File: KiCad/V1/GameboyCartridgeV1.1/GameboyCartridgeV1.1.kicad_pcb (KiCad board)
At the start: 2 copper layers, 52.8 x 61.2 mm, 58 parts, among them J1 USB_C_Receptacle_USB2.0, J2 DBG_UART, J3 Conn_01x06, Q1 CJ2302, SW1 SW_Push, U1 W25Q128JVS, U2 RP2040, U3 CartBus, U5 TXB0102DCU, U6 TXB0108PW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

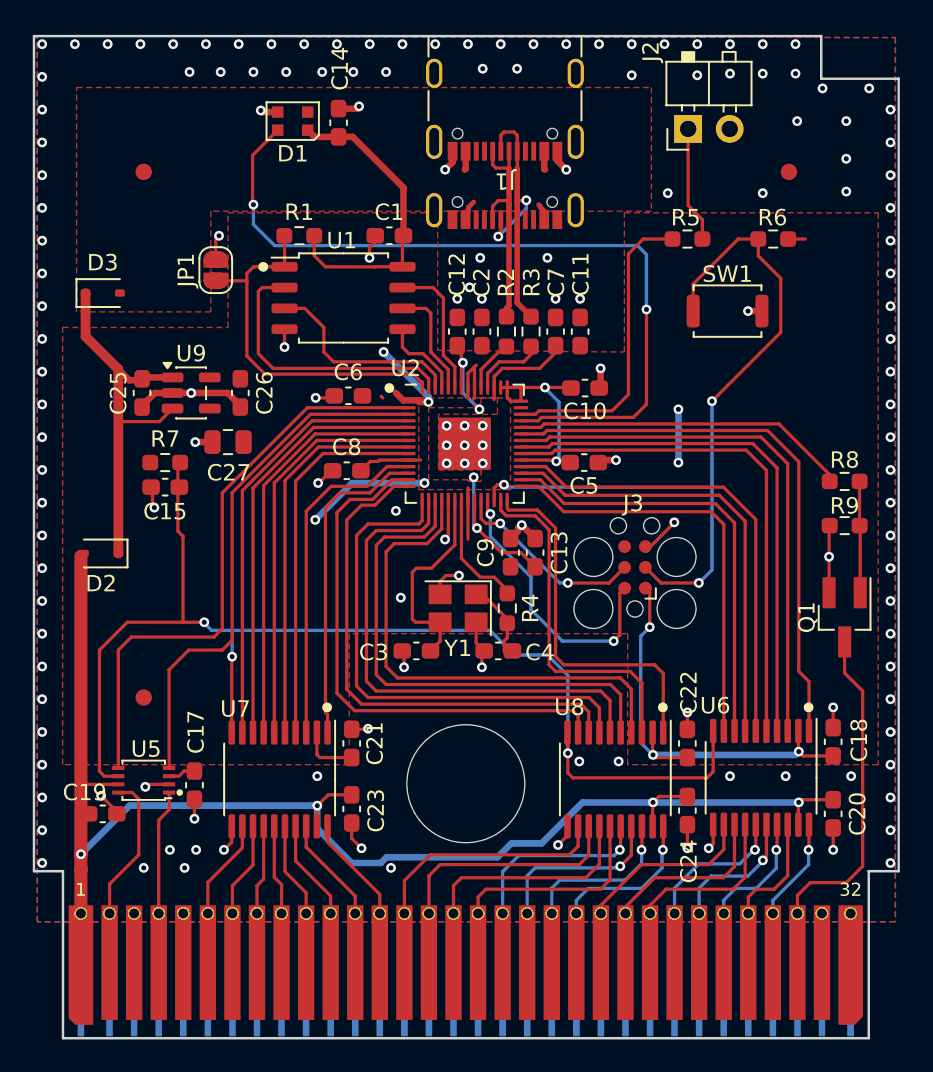
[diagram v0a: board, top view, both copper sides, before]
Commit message: usb port placement
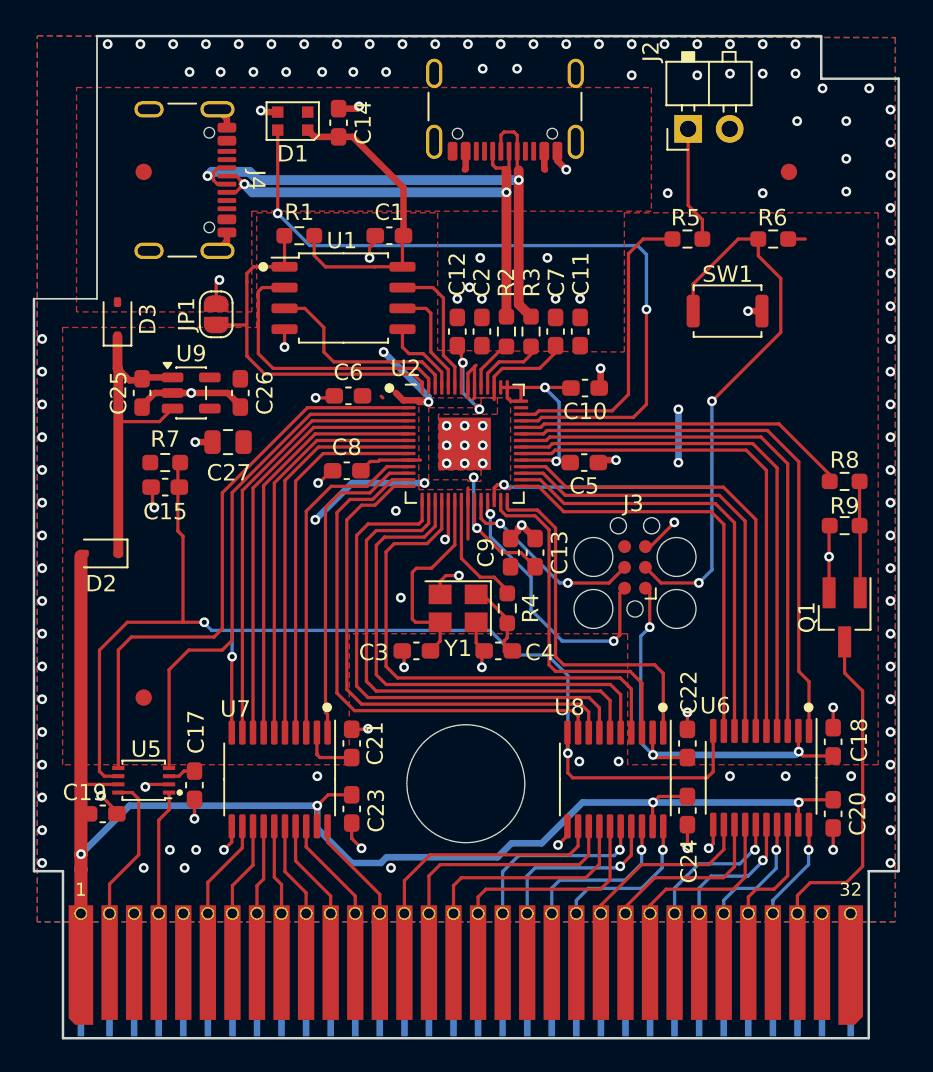
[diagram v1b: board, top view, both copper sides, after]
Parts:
- added J4: USB_C_Receptacle_USB2.0, Connector_USB:USB_C_Receptacle_GCT_USB4105-xx-A_16P_TopMnt_Horizontal, F.Cu at (93.5, 64.5)
- moved JP1 2.70 mm to (96.5, 72.7)
- moved D3 1.84 mm to (90.5, 73.0), turned to 90 degrees
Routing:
- net USB_D-: track 18.4 -> 35.6 mm
- net USB_D+: track 14.0 -> 30.8 mm, vias 0 -> 2
- net +5V: track 24.0 -> 20.6 mm
- net LED_DIN: track 48.4 -> 45.9 mm
- net VBUS: track 4.62 -> 2.29 mm
- net GND: track 58.8 -> 60.2 mm, vias 158 -> 147
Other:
- outline, holes or cut-outs redrawn
